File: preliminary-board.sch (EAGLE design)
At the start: 3 parts, among them U1 STM32F042K6

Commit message: make preliminary schematic much more interesting
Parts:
- added C1, C2, C3: 33pf, rcl:C-EUC0805
- added D1, D2: (no value), SparkFun-LED:LED10MM
- added JP2: (no value), pinhead:PINHD-1X2
- added JP3: (no value), pinhead:PINHD-1X5
- added R2: 6k, rcl:R-US_R0805
- added R3, R4: 330, rcl:R-US_R0805
- added R5, R6, R7: 10k, rcl:R-US_R0805
- added S1, S2, S3: SPST, SparkFun-Switches:MOMENTARY-SWITCH-SPST-PTH-6.0MM
- added Y1: 8MHz, SparkFun-Clocks:CRYSTAL-8MHZSMD-HC49UP
- R1: value (none) -> 6k
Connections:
- new net AVDD: U1.VDDA
- new net BOOT0: R7.1, U1.PB8-BOOT0
- new net BUT1: R5.1, S1.1, U1.PB3
- new net BUT2: R6.1, S2.1, U1.PB4
- new net N$2: JP2.2, R2.2, U1.PA1
- new net N$3: R3.1, U1.PB0
- new net N$4: R4.1, U1.PB1
- new net N$5: D1.A, R3.2
- new net N$6: D2.A, R4.2
- new net NRST: C3.1, JP3.1, S3.2, U1.NRST
- new net OSC_IN: C2.1, U1.PF0-OSC_IN, Y1.2
- new net OSC_OUT: C1.1, U1.PF1-OSC_OUT, Y1.1
- new net SWCLK: JP3.2, U1.PA14-SWCLK
- new net SWDIO: JP3.4, U1.PA13-SWDIO
- new net USBM: U1.PA10
- new net USBP: U1.PA9
- net 3.3V: now also JP2.1, JP3.5, S1.2, S2.2, U1.VDD
- net GND: now also C1.2, C2.2, C3.2, D1.C, D2.C, JP3.3, R2.1, R5.2, R6.2, R7.2, S3.1, U1.VSS
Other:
- moved on the sheet: JP1, R1

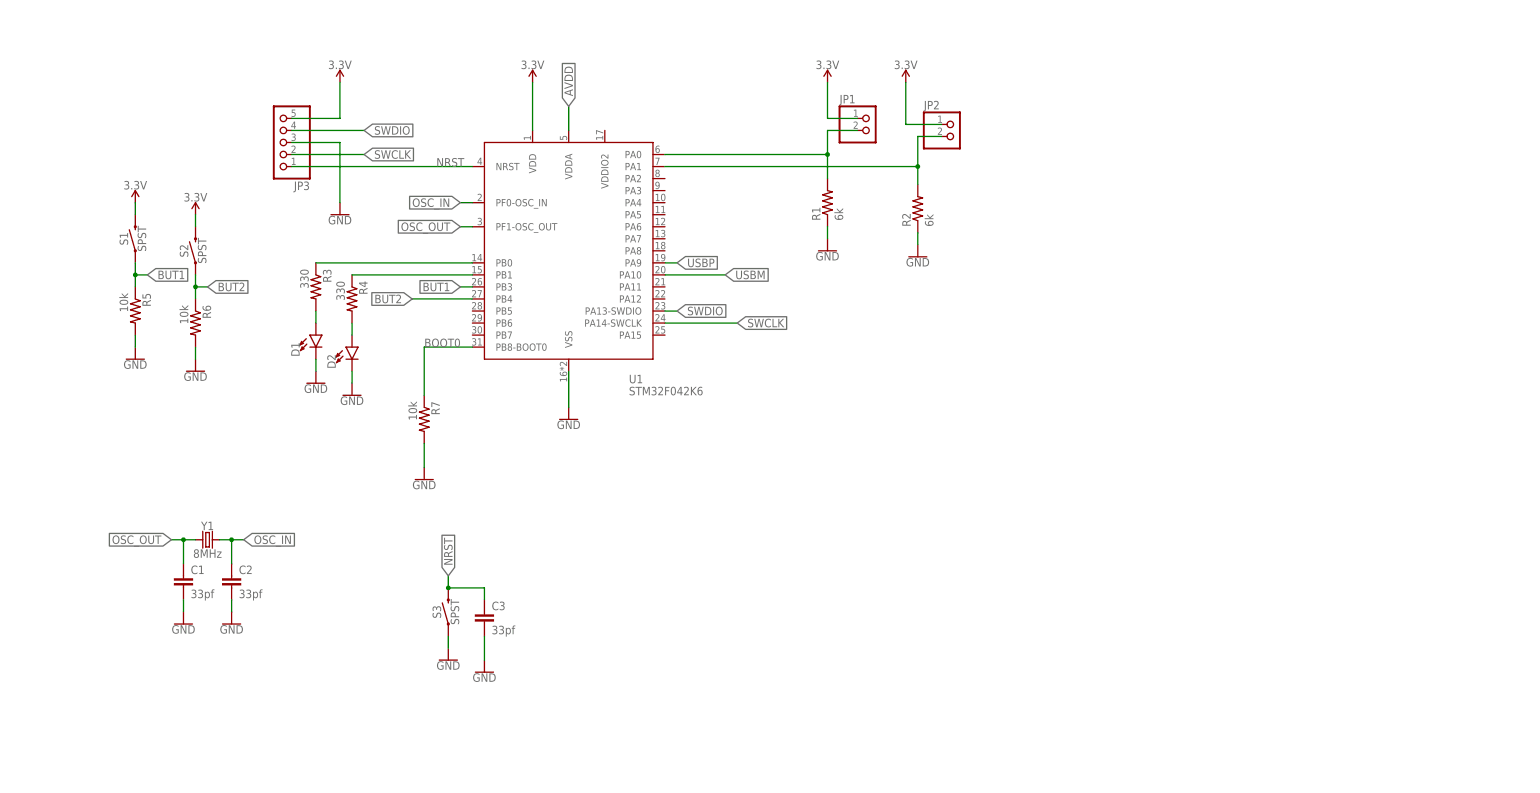
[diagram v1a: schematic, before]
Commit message: finished preliminary board BASED OFF OF http://ebrombaugh.studionebula.com/embedded/stm32f042breakout/stm32f042f_breakout_schematic.pdf
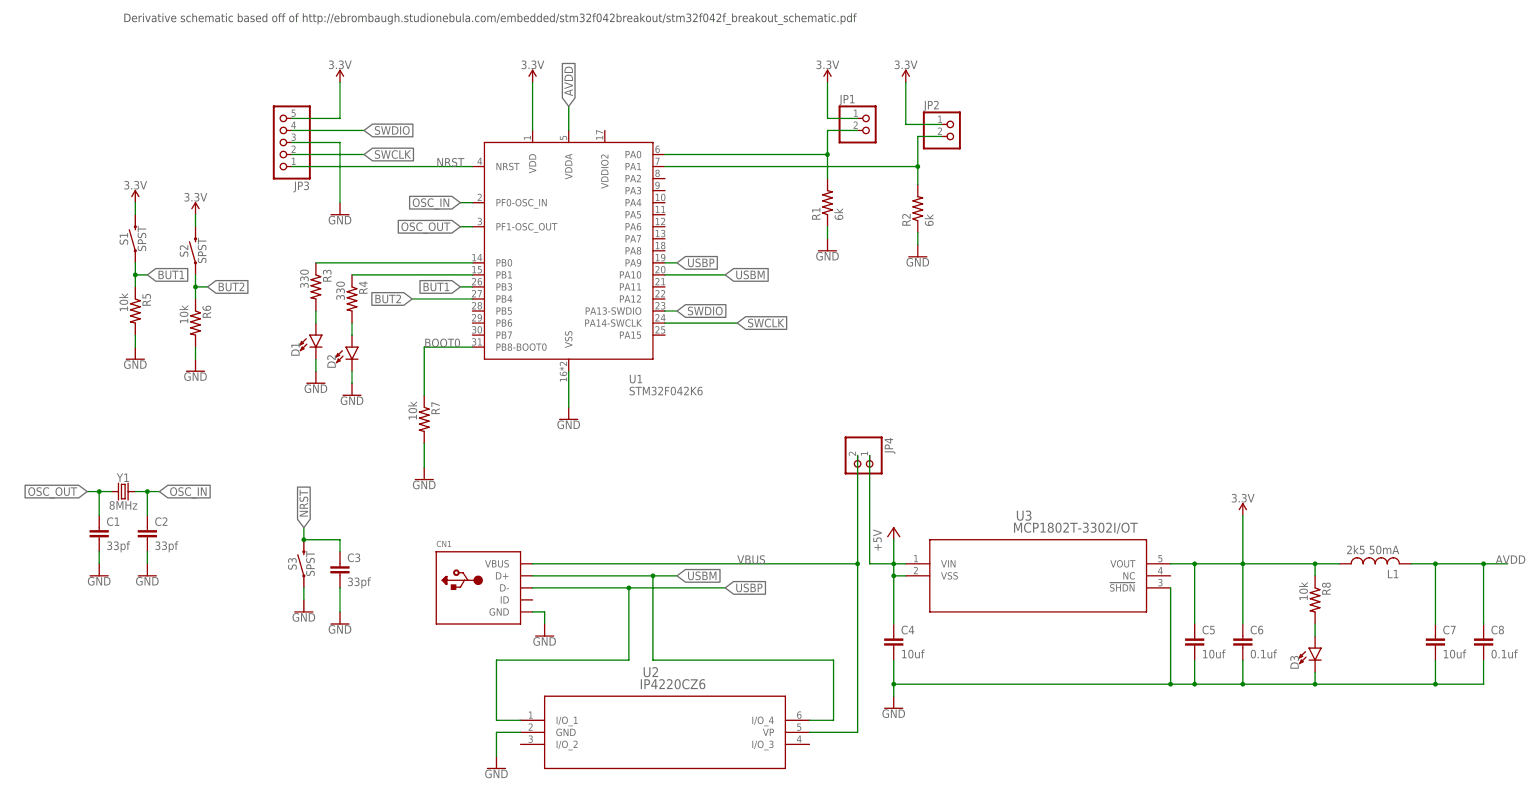
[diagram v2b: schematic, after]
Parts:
- added C4, C5, C7: 10uf, rcl:C-EUC0805
- added C6, C8: 0.1uf, rcl:C-EUC0805
- added CN1: (no value), adafruit:USBMOLEX
- added D3: (no value), SparkFun-LED:LED10MM
- added JP4: (no value), pinhead:PINHD-1X2
- added L1: 2k5 50mA, rcl:L-USL3216C
- added R8: 10k, rcl:R-US_R0805
- added U2: IP4220CZ6, IP4220CZ6:IP4220CZ6
- added U3: MCP1802T-3302I/OT, MCP1802T:MCP1802T-3302I/OT
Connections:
- new net +5V: C4.1, JP4.1, U3.VIN, U3.VSS
- new net N$9: D3.A, R8.2
- new net VBUS: CN1.VBUS, JP4.2, U2.VP
- net 3.3V: now also C5.1, C6.1, L1.1, R8.1, U3.VOUT
- net AVDD: now also C7.1, C8.1, L1.2
- net GND: now also C4.2, C5.2, C6.2, C7.2, C8.2, CN1.GND, D3.C, U2.GND, U3.!SHDN
- net USBM: now also CN1.D+, U2.I/O_4
- net USBP: now also CN1.D-, U2.I/O_1
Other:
- note added: "Derivative schematic based off of http://ebrombaugh.studionebula.com/embedded/stm32f042breakout/stm32f042f_breakout_schematic.pdf"
- moved on the sheet: C1, C2, C3, S3, Y1
